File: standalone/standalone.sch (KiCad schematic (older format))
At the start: 4 parts

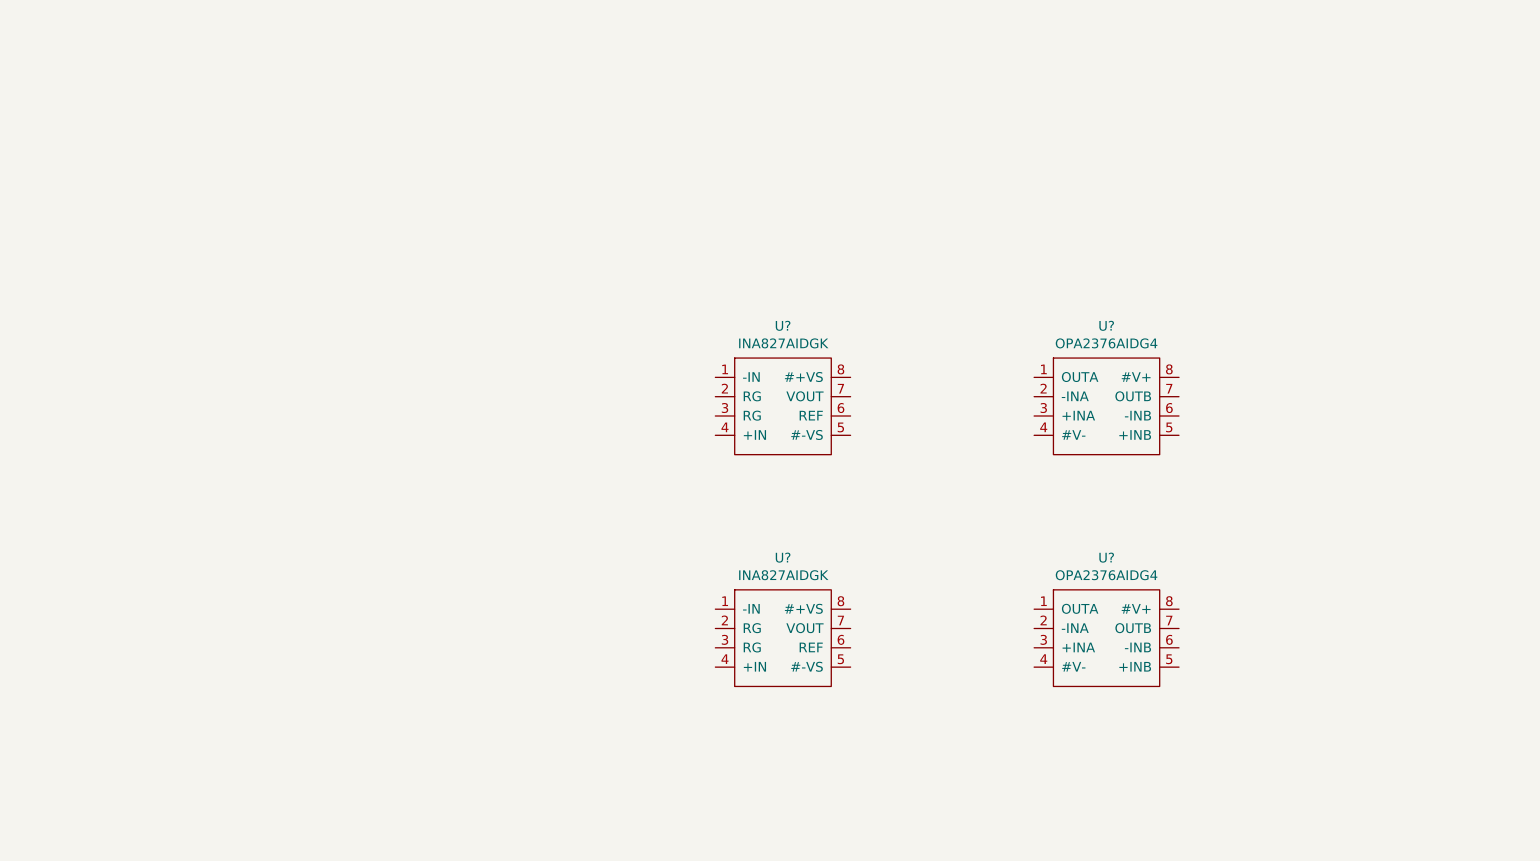
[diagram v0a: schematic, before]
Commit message: schematic completed
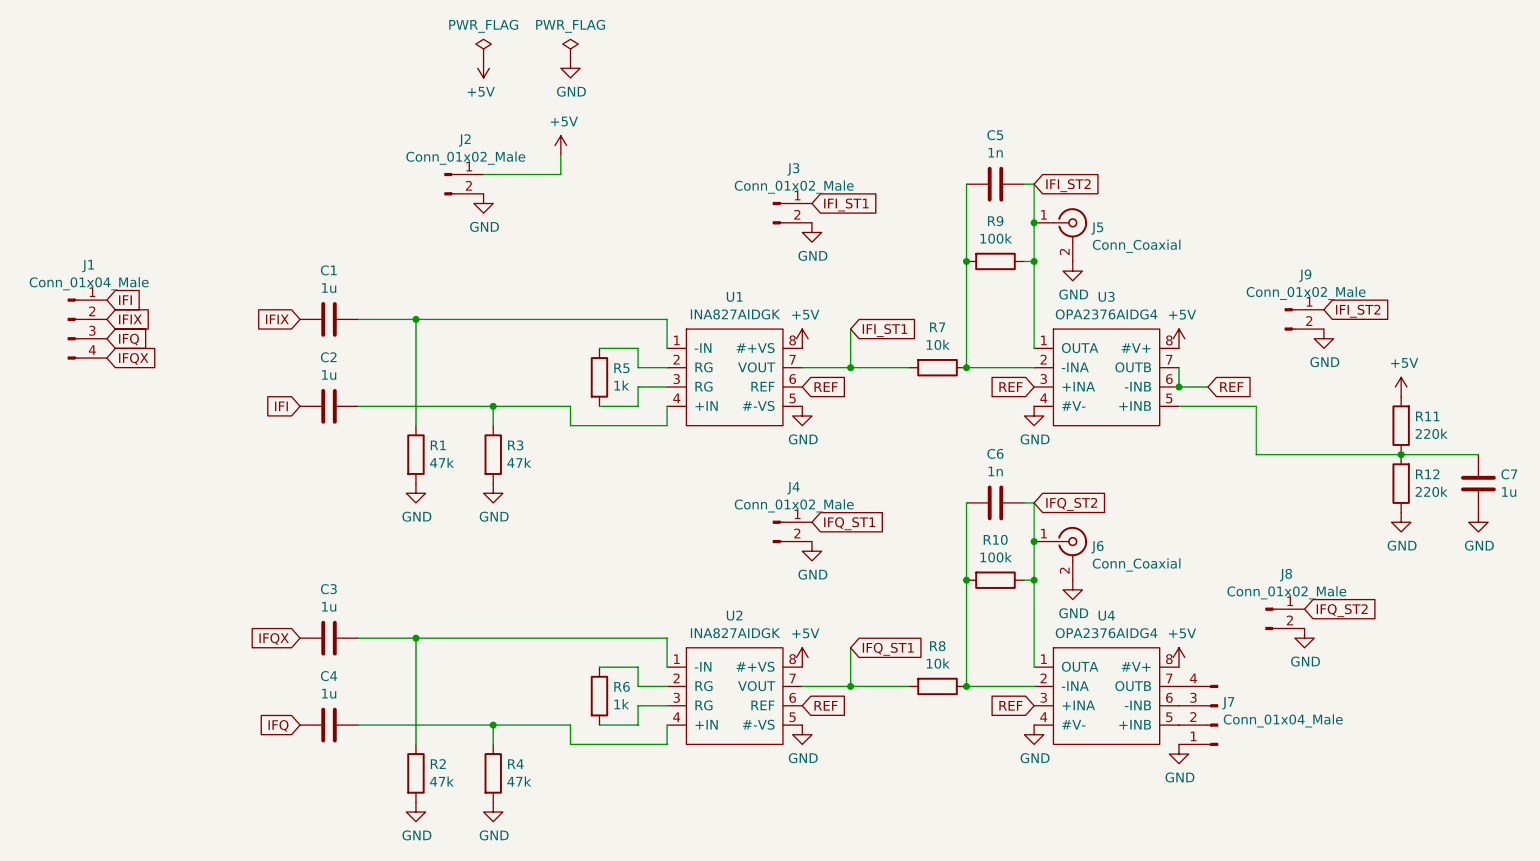
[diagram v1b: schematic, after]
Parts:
- removed U?: INA827AIDGK, Package_SO:VSSOP-8_3.0x3.0mm_P0.65mm, symbol backend:INA827AIDGK
- removed U?: OPA2376AIDG4, Package_SO:SOIC-8_3.9x4.9mm_P1.27mm, symbol backend:OPA2376AIDG4
- added C1, C2, C3, C4, C7: 1u, Capacitor_SMD:C_0603_1608Metric_Pad1.08x0.95mm_HandSolder, symbol Device:C
- added C5, C6: 1n, Capacitor_SMD:C_0603_1608Metric_Pad1.08x0.95mm_HandSolder, symbol Device:C
- added J1: Conn_01x04_Male, Connector_PinHeader_2.54mm:PinHeader_1x04_P2.54mm_Vertical, symbol Connector:Conn_01x04_Male
- added J2, J3, J4, J8, J9: Conn_01x02_Male, Connector_PinHeader_2.54mm:PinHeader_1x02_P2.54mm_Vertical, symbol Connector:Conn_01x02_Male
- added J5, J6: Conn_Coaxial, Connector_Coaxial:BNC_Amphenol_B6252HB-NPP3G-50_Horizontal, symbol Connector:Conn_Coaxial
- added J7: Conn_01x04_Male, Connector_PinSocket_2.54mm:PinSocket_1x04_P2.54mm_Vertical, symbol Connector:Conn_01x04_Male
- added R1, R2, R3, R4: 47k, Resistor_SMD:R_0603_1608Metric_Pad0.98x0.95mm_HandSolder, symbol Device:R
- added R10, R9: 100k, Resistor_SMD:R_0603_1608Metric_Pad0.98x0.95mm_HandSolder, symbol Device:R
- added R11, R12: 220k, Resistor_SMD:R_0603_1608Metric_Pad0.98x0.95mm_HandSolder, symbol Device:R
- added R5, R6: 1k, Resistor_SMD:R_0603_1608Metric_Pad0.98x0.95mm_HandSolder, symbol Device:R
- added R7, R8: 10k, Resistor_SMD:R_0603_1608Metric_Pad0.98x0.95mm_HandSolder, symbol Device:R
- added U2: INA827AIDGK, Package_SO:VSSOP-8_3.0x3.0mm_P0.65mm, symbol backend:INA827AIDGK
- added U4: OPA2376AIDG4, Package_SO:SOIC-8_3.9x4.9mm_P1.27mm, symbol backend:OPA2376AIDG4
- gave numbers to parts that had none: 2
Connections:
- net at U1.1 (-IN): now also C1.1, R1.1
- net at U1.2 (RG): now also R5.1
- net at U1.3 (RG): now also R5.2
- net at U1.4 (+IN): now also C2.1, R3.1
- net GND: now reaches U1.5 (#-VS)
- net GND: now also U3.4 (#V-), C7.1, J2.2 (Pin_2), J3.2 (Pin_2), J4.2 (Pin_2), J5.2 (Ext), J6.2 (Ext), J7.1 (Pin_1), J8.2 (Pin_2), J9.2 (Pin_2), R1.2, R12.1, R2.2, R3.2, R4.2, U2.5 (#-VS), U4.4 (#V-)
- net REF: now reaches U1.6 (REF)
- net REF: now also U3.3 (+INA), U3.6 (-INB), U3.7 (OUTB), U2.6 (REF), U4.3 (+INA)
- net IFI_ST1: now reaches U1.7 (VOUT)
- net IFI_ST1: now also J3.1 (Pin_1), R7.2
- net +5V: now reaches U1.8 (#+VS)
- net +5V: now also U3.8 (#V+), J2.1 (Pin_1), R11.2, U2.8 (#+VS), U4.8 (#V+)
- net IFI_ST2: now reaches U3.1 (OUTA)
- net IFI_ST2: now also C5.1, J5.1 (In), J9.1 (Pin_1), R9.1
- net at U3.2 (-INA): now also C5.2, R7.1, R9.2
- net at U3.5 (+INB): now also C7.2, R11.1, R12.2
- new net: C3.1, R2.1, U2.1 (-IN)
- new net: R6.1, U2.2 (RG)
- new net: R6.2, U2.3 (RG)
- new net: C4.1, R4.1, U2.4 (+IN)
- new net: C6.2, R10.2, R8.1, U4.2 (-INA)
- new net: J7.2 (Pin_2), U4.5 (+INB)
- new net: J7.3 (Pin_3), U4.6 (-INB)
- new net: J7.4 (Pin_4), U4.7 (OUTB)
- new net IFI: C2.2, J1.1 (Pin_1)
- new net IFIX: C1.2, J1.2 (Pin_2)
- new net IFQ: C4.2, J1.3 (Pin_3)
- new net IFQX: C3.2, J1.4 (Pin_4)
- new net IFQ_ST1: J4.1 (Pin_1), R8.2, U2.7 (VOUT)
- new net IFQ_ST2: C6.1, J6.1 (In), J8.1 (Pin_1), R10.1, U4.1 (OUTA)
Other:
- moved on the sheet: U1, U3

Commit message: layout completed
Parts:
- added C10, C11, C8, C9: 100p, Capacitor_SMD:C_0603_1608Metric_Pad1.08x0.95mm_HandSolder, symbol Device:C
- J7: footprint Connector_PinSocket_2.54mm:PinSocket_1x04_P2.54mm_Vertical -> Connector_PinHeader_2.54mm:PinHeader_1x04_P2.54mm_Vertical
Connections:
- net +5V: now also C10.2, C11.2, C8.2, C9.2
- net GND: now also C10.1, C11.1, C8.1, C9.1
- net IFI: now also J1.2 (Pin_2); no longer J1.1 (Pin_1)
- net IFIX: now also J1.1 (Pin_1); no longer J1.2 (Pin_2)
- net IFQ: now also J1.4 (Pin_4); no longer J1.3 (Pin_3)
- net IFQX: now also J1.3 (Pin_3); no longer J1.4 (Pin_4)
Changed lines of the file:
@@
 	1    0    0    -1
 $EndComp
+Text GLabel 1550 2650 2    50   Input ~ 0
+IFI
 Text GLabel 1550 2550 2    50   Input ~ 0
-IFI
-Text GLabel 1550 2650 2    50   Input ~ 0
 IFIX
-Text GLabel 1550 2750 2    50   Input ~ 0
+Text GLabel 1550 2850 2    50   Input ~ 0
 IFQ
 Text GLabel 2550 3100 0    50   Input ~ 0
@@
 Text GLabel 2550 2650 0    50   Input ~ 0
 IFIX
-Text GLabel 1550 2850 2    50   Input ~ 0
+Text GLabel 1550 2750 2    50   Input ~ 0
 IFQX
 $Comp
@@
 F 0 "J7" H 7272 4632 50  0000 R CNN
 F 1 "Conn_01x04_Male" H 7272 4723 50  0000 R CNN
-F 2 "Connector_PinSocket_2.54mm:PinSocket_1x04_P2.54mm_Vertical" H 7300 4750 50  0001 C CNN
+F 2 "Connector_PinHeader_2.54mm:PinHeader_1x04_P2.54mm_Vertical" H 7300 4750 50  0001 C CNN
 F 3 "~" H 7300 4750 50  0001 C CNN
 	1    7300 4750
@@
 Wire Wire Line
 	6350 2150 6350 2350
+$Comp
+L Device:C C8
+U 1 1 61B335CB
+P 4500 2350
+F 0 "C8" V 4248 2350 50  0000 C CNN
+F 1 "100p" V 4339 2350 50  0000 C CNN
+F 2 "Capacitor_SMD:C_0603_1608Metric_Pad1.08x0.95mm_HandSolder" H 4538 2200 50  0001 C CNN
+F 3 "~" H 4500 2350 50  0001 C CNN
+	1    4500 2350
+	0    -1   -1   0
+$EndComp
+$Comp
+L power:GND #PWR0101
+U 1 1 61B34A16
+P 4350 2350
+F 0 "#PWR0101" H 4350 2100 50  0001 C CNN
+F 1 "GND" H 4355 2177 50  0000 C CNN
+F 2 "" H 4350 2350 50  0001 C CNN
+F 3 "" H 4350 2350 50  0001 C CNN
+	1    4350 2350
+	0    1    1    0
+$EndComp
+$Comp
+L Device:C C9
+U 1 1 61B3B54B
+P 4500 4000
+F 0 "C9" V 4248 4000 50  0000 C CNN
+F 1 "100p" V 4339 4000 50  0000 C CNN
+F 2 "Capacitor_SMD:C_0603_1608Metric_Pad1.08x0.95mm_HandSolder" H 4538 3850 50  0001 C CNN
+F 3 "~" H 4500 4000 50  0001 C CNN
+	1    4500 4000
+	0    -1   -1   0
+$EndComp
+$Comp
+L power:GND #PWR0102
+U 1 1 61B3B551
+P 4350 4000
+F 0 "#PWR0102" H 4350 3750 50  0001 C CNN
+F 1 "GND" H 4355 3827 50  0000 C CNN
+F 2 "" H 4350 4000 50  0001 C CNN
+F 3 "" H 4350 4000 50  0001 C CNN
+	1    4350 4000
+	0    1    1    0
+$EndComp
+$Comp
+L Device:C C11
+U 1 1 61B3D75D
+P 7150 2400
+F 0 "C11" V 6898 2400 50  0000 C CNN
+F 1 "100p" V 6989 2400 50  0000 C CNN
+F 2 "Capacitor_SMD:C_0603_1608Metric_Pad1.08x0.95mm_HandSolder" H 7188 2250 50  0001 C CNN
+F 3 "~" H 7150 2400 50  0001 C CNN
+	1    7150 2400
+	0    -1   -1   0
+$EndComp
+$Comp
+L power:GND #PWR0103
+U 1 1 61B3D763
+P 7000 2400
+F 0 "#PWR0103" H 7000 2150 50  0001 C CNN
+F 1 "GND" H 7005 2227 50  0000 C CNN
+F 2 "" H 7000 2400 50  0001 C CNN
+F 3 "" H 7000 2400 50  0001 C CNN
+	1    7000 2400
+	0    1    1    0
+$EndComp
+$Comp
+L Device:C C10
+U 1 1 61B3F285
+P 7100 4050
+F 0 "C10" V 6848 4050 50  0000 C CNN
+F 1 "100p" V 6939 4050 50  0000 C CNN
+F 2 "Capacitor_SMD:C_0603_1608Metric_Pad1.08x0.95mm_HandSolder" H 7138 3900 50  0001 C CNN
+F 3 "~" H 7100 4050 50  0001 C CNN
+	1    7100 4050
+	0    -1   -1   0
+$EndComp
+$Comp
+L power:GND #PWR0104
+U 1 1 61B3F28B
+P 6950 4050
+F 0 "#PWR0104" H 6950 3800 50  0001 C CNN
+F 1 "GND" H 6955 3877 50  0000 C CNN
+F 2 "" H 6950 4050 50  0001 C CNN
+F 3 "" H 6950 4050 50  0001 C CNN
+	1    6950 4050
+	0    1    1    0
+$EndComp
+Wire Wire Line
+	4650 2350 5250 2350
+Wire Wire Line
+	5250 2350 5250 2800
+Wire Wire Line
+	5250 2800 5150 2800
+Connection ~ 5150 2800
+Wire Wire Line
+	4650 4000 5250 4000
+Wire Wire Line
+	5250 4000 5250 4450
+Wire Wire Line
+	5250 4450 5150 4450
+Connection ~ 5150 4450
+Wire Wire Line
+	7250 4050 7250 4450
+Wire Wire Line
+	7250 4450 7100 4450
+Connection ~ 7100 4450
+Wire Wire Line
+	7300 2400 7300 2800
+Wire Wire Line
+	7300 2800 7100 2800
+Connection ~ 7100 2800
 $EndSCHEMATC

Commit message: bom
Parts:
- U1, U2: symbol backend:INA827AIDGK -> standalone-rescue:INA827AIDGK-backend
- U3, U4: symbol backend:OPA2376AIDG4 -> standalone-rescue:OPA2376AIDG4-backend
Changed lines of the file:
@@
 $EndDescr
 $Comp
-L backend:INA827AIDGK U1
+L standalone-rescue:INA827AIDGK-backend U1
 U 1 1 61A91117
 P 4800 3150
@@
 $EndComp
 $Comp
-L backend:OPA2376AIDG4 U3
+L standalone-rescue:OPA2376AIDG4-backend U3
 U 1 1 61A95643
 P 6600 3250
@@
 $EndComp
 $Comp
-L backend:INA827AIDGK U2
+L standalone-rescue:INA827AIDGK-backend U2
 U 1 1 61B52794
 P 4800 4800
@@
 $EndComp
 $Comp
-L backend:OPA2376AIDG4 U4
+L standalone-rescue:OPA2376AIDG4-backend U4
 U 1 1 61B5279A
 P 6600 4900
